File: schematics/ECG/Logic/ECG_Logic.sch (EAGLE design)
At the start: 77 parts, among them IC1 ADS1293, IC10 FSA4157, IC2 LIS3DH, IC3 MCP1703, IC4 CC2541, IC5 FSA4157, IC6 FSA4157, IC7 FSA4157, IC8 BALUN_2450BM_SERIES_SMD, IC9 LTC6907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

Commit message: added board detect pin, need to find proper place to route trace
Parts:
- added U$7: TARGET_RA, pins:TARGET_RA
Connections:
- new net BOARD_DETECT: U$7.1
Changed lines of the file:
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@@
 <grid distance="0.1" unitdist="inch" unit="inch" style="lines" multiple="1" display="no" altdistance="0.01" altunitdist="inch" altunit="inch"/>
 <layers>
-<layer number="1" name="Top" color="4" fill="1" visible="yes" active="no"/>
-<layer number="2" name="Route2" color="1" fill="3" visible="yes" active="no"/>
-<layer number="3" name="Route3" color="4" fill="3" visible="yes" active="no"/>
-<layer number="4" name="Route4" color="1" fill="4" visible="yes" active="no"/>
-<layer number="5" name="Route5" color="4" fill="4" visible="yes" active="no"/>
-<layer number="6" name="Route6" color="1" fill="8" visible="yes" active="no"/>
-<layer number="7" name="Route7" color="4" fill="8" visible="yes" active="no"/>
-<layer number="8" name="Route8" color="1" fill="2" visible="yes" active="no"/>
-<layer number="9" name="Route9" color="4" fill="2" visible="yes" active="no"/>
-<layer number="10" name="Route10" color="1" fill="7" visible="yes" active="no"/>
-<layer number="11" name="Route11" color="4" fill="7" visible="yes" active="no"/>
-<layer number="12" name="Route12" color="1" fill="5" visible="yes" active="no"/>
-<layer number="13" name="Route13" color="4" fill="5" visible="yes" active="no"/>
-<layer number="14" name="Route14" color="1" fill="6" visible="yes" active="no"/>
-<layer number="15" name="Route15" color="4" fill="6" visible="yes" active="no"/>
-<layer number="16" name="Bottom" color="1" fill="1" visible="yes" active="no"/>
-<layer number="17" name="Pads" color="2" fill="1" visible="yes" active="no"/>
-<layer number="18" name="Vias" color="2" fill="1" visible="yes" active="no"/>
-<layer number="19" name="Unrouted" color="6" fill="1" visible="yes" active="no"/>
-<layer number="20" name="Dimension" color="15" fill="1" visible="yes" active="no"/>
-<layer number="21" name="tPlace" color="7" fill="1" visible="yes" active="no"/>
-<layer number="22" name="bPlace" color="7" fill="1" visible="yes" active="no"/>
-<layer number="23" name="tOrigins" color="15" fill="1" visible="yes" active="no"/>
-<layer number="24" name="bOrigins" color="15" fill="1" visible="yes" active="no"/>
-<layer number="25" name="tNames" color="7" fill="1" visible="yes" active="no"/>
-<layer number="26" name="bNames" color="7" fill="1" visible="yes" active="no"/>
-<layer number="27" name="tValues" color="7" fill="1" visible="yes" active="no"/>
-<layer number="28" name="bValues" color="7" fill="1" visible="yes" active="no"/>
+<layer number="1" name="Top" color="4" fill="1" visible="no" active="no"/>
+<layer number="2" name="Route2" color="1" fill="3" visible="no" active="no"/>
+<layer number="3" name="Route3" color="4" fill="3" visible="no" active="no"/>
+<layer number="4" name="Route4" color="1" fill="4" visible="no" active="no"/>
+<layer number="5" name="Route5" color="4" fill="4" visible="no" active="no"/>
+<layer number="6" name="Route6" color="1" fill="8" visible="no" active="no"/>
+<layer number="7" name="Route7" color="4" fill="8" visible="no" active="no"/>
+<layer number="8" name="Route8" color="1" fill="2" visible="no" active="no"/>
+<layer number="9" name="Route9" color="4" fill="2" visible="no" active="no"/>
+<layer number="10" name="Route10" color="1" fill="7" visible="no" active="no"/>
+<layer number="11" name="Route11" color="4" fill="7" visible="no" active="no"/>
+<layer number="12" name="Route12" color="1" fill="5" visible="no" active="no"/>
+<layer number="13" name="Route13" color="4" fill="5" visible="no" active="no"/>
+<layer number="14" name="Route14" color="1" fill="6" visible="no" active="no"/>
+<layer number="15" name="Route15" color="4" fill="6" visible="no" active="no"/>
+<layer number="16" name="Bottom" color="1" fill="1" visible="no" active="no"/>
+<layer number="17" name="Pads" color="2" fill="1" visible="no" active="no"/>
+<layer number="18" name="Vias" color="2" fill="1" visible="no" active="no"/>
+<layer number="19" name="Unrouted" color="6" fill="1" visible="no" active="no"/>
+<layer number="20" name="Dimension" color="15" fill="1" visible="no" active="no"/>
+<layer number="21" name="tPlace" color="7" fill="1" visible="no" active="no"/>
+<layer number="22" name="bPlace" color="7" fill="1" visible="no" active="no"/>
+<layer number="23" name="tOrigins" color="15" fill="1" visible="no" active="no"/>
+<layer number="24" name="bOrigins" color="15" fill="1" visible="no" active="no"/>
+<layer number="25" name="tNames" color="7" fill="1" visible="no" active="no"/>
+<layer number="26" name="bNames" color="7" fill="1" visible="no" active="no"/>
+<layer number="27" name="tValues" color="7" fill="1" visible="no" active="no"/>
+<layer number="28" name="bValues" color="7" fill="1" visible="no" active="no"/>
 <layer number="29" name="tStop" color="7" fill="3" visible="no" active="no"/>
 <layer number="30" name="bStop" color="7" fill="6" visible="no" active="no"/>
@@
 <layer number="35" name="tGlue" color="7" fill="4" visible="no" active="no"/>
 <layer number="36" name="bGlue" color="7" fill="5" visible="no" active="no"/>
-<layer number="37" name="tTest" color="7" fill="1" visible="yes" active="no"/>
-<layer number="38" name="bTest" color="7" fill="1" visible="yes" active="no"/>
+<layer number="37" name="tTest" color="7" fill="1" visible="no" active="no"/>
+<layer number="38" name="bTest" color="7" fill="1" visible="no" active="no"/>
 <layer number="39" name="tKeepout" color="4" fill="11" visible="no" active="no"/>
 <layer number="40" name="bKeepout" color="1" fill="11" visible="no" active="no"/>
@@
 <layer number="44" name="Drills" color="7" fill="1" visible="no" active="no"/>
 <layer number="45" name="Holes" color="7" fill="1" visible="no" active="no"/>
-<layer number="46" name="Milling" color="3" fill="1" visible="yes" active="no"/>
-<layer number="47" name="Measures" color="7" fill="1" visible="yes" active="no"/>
-<layer number="48" name="Document" color="7" fill="1" visible="yes" active="no"/>
-<layer number="49" name="Reference" color="7" fill="1" visible="yes" active="no"/>
-<layer number="50" name="dxf" color="7" fill="1" visible="yes" active="no"/>
-<layer number="51" name="tDocu" color="7" fill="1" visible="yes" active="no"/>
-<layer number="52" name="bDocu" color="7" fill="1" visible="yes" active="no"/>
-<layer number="53" name="tGND_GNDA" color="7" fill="9" visible="yes" active="no"/>
-<layer number="54" name="bGND_GNDA" color="1" fill="9" visible="yes" active="no"/>
-<layer number="56" name="wert" color="7" fill="1" visible="yes" active="no"/>
+<layer number="46" name="Milling" color="3" fill="1" visible="no" active="no"/>
+<layer number="47" name="Measures" color="7" fill="1" visible="no" active="no"/>
+<layer number="48" name="Document" color="7" fill="1" visible="no" active="no"/>
+<layer number="49" name="Reference" color="7" fill="1" visible="no" active="no"/>
+<layer number="50" name="dxf" color="7" fill="1" visible="no" active="no"/>
+<layer number="51" name="tDocu" color="7" fill="1" visible="no" active="no"/>
+<layer number="52" name="bDocu" color="7" fill="1" visible="no" active="no"/>
+<layer number="53" name="tGND_GNDA" color="7" fill="9" visible="no" active="no"/>
+<layer number="54" name="bGND_GNDA" color="1" fill="9" visible="no" active="no"/>
+<layer number="56" name="wert" color="7" fill="1" visible="no" active="no"/>
 <layer number="91" name="Nets" color="2" fill="1" visible="yes" active="yes"/>
 <layer number="92" name="Busses" color="1" fill="1" visible="yes" active="yes"/>
@@
 <part name="IC10" library="fairchild" deviceset="FSA4157" device=""/>
 <part name="GND17" library="supply1" deviceset="GND" device=""/>
+<part name="U$7" library="pins" deviceset="TARGET_RA" device=""/>
 </parts>
 <sheets>
@@
 <instance part="IC10" gate="FSA4157" x="68.58" y="162.56"/>
 <instance part="GND17" gate="1" x="55.88" y="157.48"/>
+<instance part="U$7" gate="PIN" x="187.96" y="187.96"/>
 </instances>
 <busses>
@@
 </segment>
 </net>
+<net name="BOARD_DETECT" class="0">
+<segment>
+<pinref part="U$7" gate="PIN" pin="1"/>
+<wire x1="182.88" y1="187.96" x2="180.34" y2="187.96" width="0.1524" layer="91"/>
+<junction x="182.88" y="187.96"/>
+<label x="165.1" y="187.96" size="1.27" layer="95"/>
+</segment>
+</net>

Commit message: routed detect pin to cc2541
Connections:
- net BOARD_DETECT: now also IC4.SCL
- net OSC_SW_VCC: now also IC4.SDA; no longer IC4.SCL
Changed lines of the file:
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@@
 <?xml version="1.0" encoding="utf-8"?>
 <!DOCTYPE eagle SYSTEM "eagle.dtd">
-<eagle version="6.4">
+<eagle version="6.5.0">
 <drawing>
 <settings>
@@
 <net name="OSC_SW_VCC" class="0">
 <segment>
+<pinref part="IC10" gate="FSA4157" pin="S"/>
+<junction x="81.28" y="165.1"/>
+<wire x1="81.28" y1="165.1" x2="83.82" y2="165.1" width="0.1524" layer="91"/>
+<label x="83.82" y="165.1" size="1.27" layer="95"/>
+</segment>
+<segment>
+<pinref part="IC4" gate="G$1" pin="SDA"/>
+<wire x1="205.74" y1="76.2" x2="203.2" y2="76.2" width="0.1524" layer="91"/>
+<junction x="205.74" y="76.2"/>
+<label x="190.5" y="76.2" size="1.27" layer="95"/>
+</segment>
+</net>
+<net name="OSC_VCC" class="0">
+<segment>
+<pinref part="C1" gate="G$1" pin="1"/>
+<wire x1="147.32" y1="137.16" x2="144.78" y2="137.16" width="0.1524" layer="91"/>
+<junction x="147.32" y="137.16"/>
+<label x="137.16" y="137.16" size="1.27" layer="95"/>
+</segment>
+<segment>
+<pinref part="IC9" gate="IC" pin="V+"/>
+<wire x1="134.62" y1="116.84" x2="132.08" y2="116.84" width="0.1524" layer="91"/>
+<junction x="134.62" y="116.84"/>
+<label x="124.46" y="116.84" size="1.27" layer="95"/>
+</segment>
+<segment>
+<pinref part="IC10" gate="FSA4157" pin="A"/>
+<junction x="81.28" y="160.02"/>
+<wire x1="81.28" y1="160.02" x2="83.82" y2="160.02" width="0.1524" layer="91"/>
+<label x="83.82" y="160.02" size="1.27" layer="95"/>
+</segment>
+</net>
+<net name="BOARD_DETECT" class="0">
+<segment>
+<pinref part="U$7" gate="PIN" pin="1"/>
+<wire x1="182.88" y1="187.96" x2="180.34" y2="187.96" width="0.1524" layer="91"/>
+<junction x="182.88" y="187.96"/>
+<label x="165.1" y="187.96" size="1.27" layer="95"/>
+</segment>
+<segment>
 <pinref part="IC4" gate="G$1" pin="SCL"/>
 <wire x1="205.74" y1="78.74" x2="203.2" y2="78.74" width="0.1524" layer="91"/>
@@
 <label x="190.5" y="78.74" size="1.27" layer="95"/>
 </segment>
-<segment>
-<pinref part="IC10" gate="FSA4157" pin="S"/>
-<junction x="81.28" y="165.1"/>
-<wire x1="81.28" y1="165.1" x2="83.82" y2="165.1" width="0.1524" layer="91"/>
-<label x="83.82" y="165.1" size="1.27" layer="95"/>
-</segment>
-</net>
-<net name="OSC_VCC" class="0">
-<segment>
-<pinref part="C1" gate="G$1" pin="1"/>
-<wire x1="147.32" y1="137.16" x2="144.78" y2="137.16" width="0.1524" layer="91"/>
-<junction x="147.32" y="137.16"/>
-<label x="137.16" y="137.16" size="1.27" layer="95"/>
-</segment>
-<segment>
-<pinref part="IC9" gate="IC" pin="V+"/>
-<wire x1="134.62" y1="116.84" x2="132.08" y2="116.84" width="0.1524" layer="91"/>
-<junction x="134.62" y="116.84"/>
-<label x="124.46" y="116.84" size="1.27" layer="95"/>
-</segment>
-<segment>
-<pinref part="IC10" gate="FSA4157" pin="A"/>
-<junction x="81.28" y="160.02"/>
-<wire x1="81.28" y1="160.02" x2="83.82" y2="160.02" width="0.1524" layer="91"/>
-<label x="83.82" y="160.02" size="1.27" layer="95"/>
-</segment>
-</net>
-<net name="BOARD_DETECT" class="0">
-<segment>
-<pinref part="U$7" gate="PIN" pin="1"/>
-<wire x1="182.88" y1="187.96" x2="180.34" y2="187.96" width="0.1524" layer="91"/>
-<junction x="182.88" y="187.96"/>
-<label x="165.1" y="187.96" size="1.27" layer="95"/>
-</segment>
-</net>
+</net>

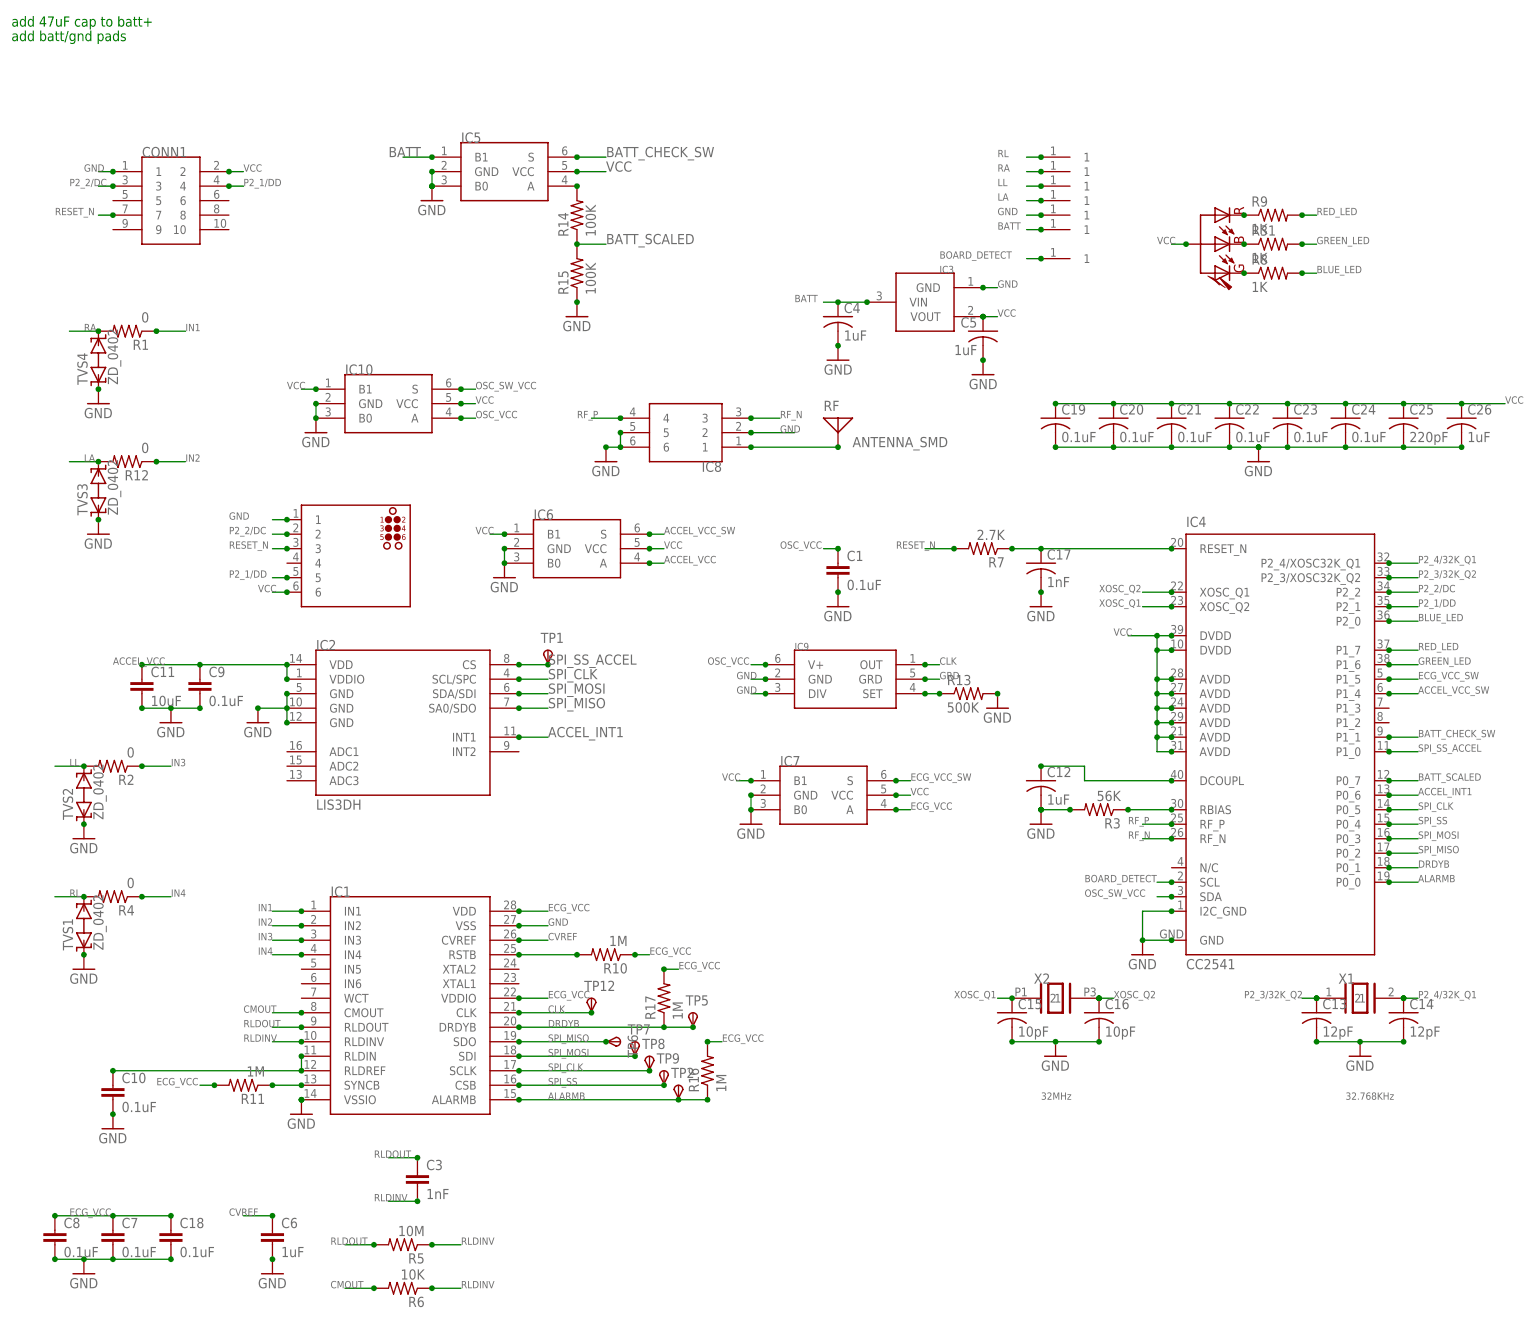
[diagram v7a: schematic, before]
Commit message: added new low profile 4Mhz xtal
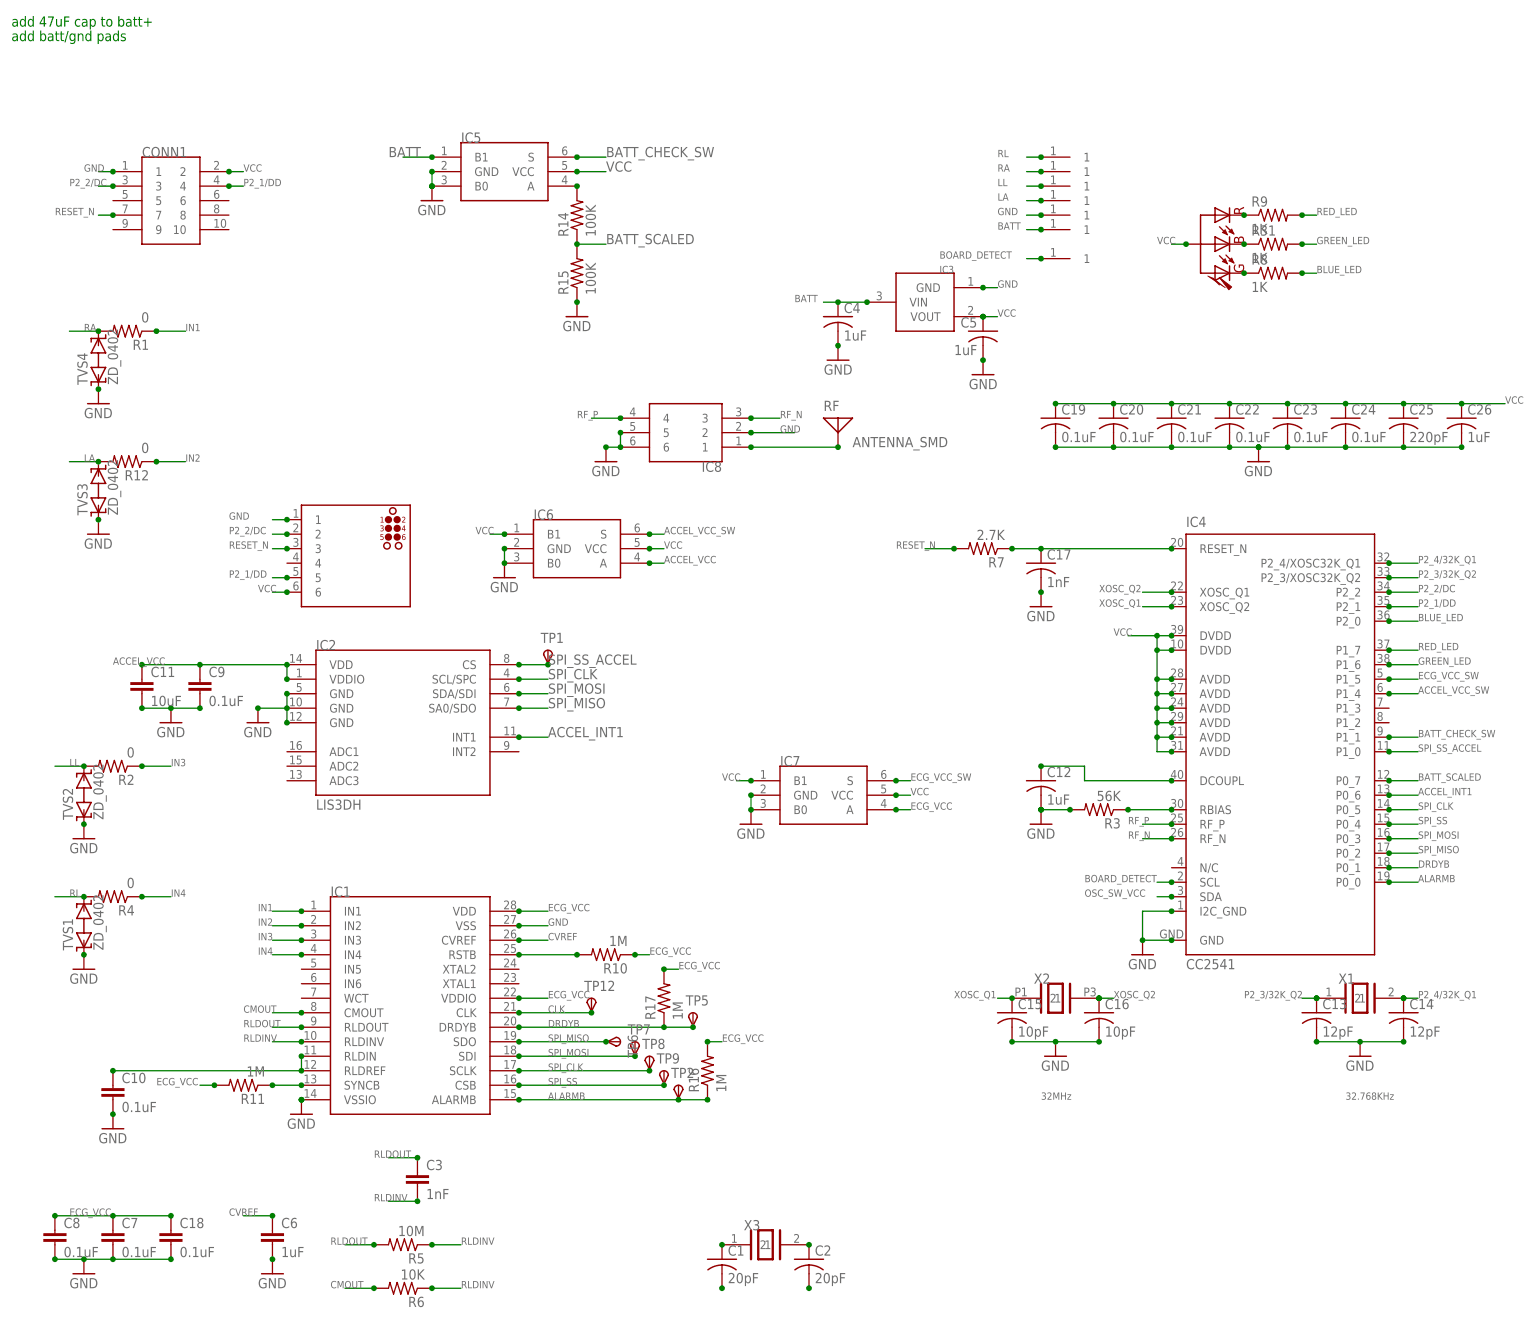
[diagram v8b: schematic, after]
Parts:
- removed IC10: FSA4157, fairchild:FSA4157
- removed IC9: LTC6907, linear:LTC6907
- removed R13: 500K, rcl:R-US_R1206
- added C2: 20pF, rcl:C-USC0201
- added X3: ECS-40-20-4VX, ecs:ECS-40-20-4VX
- C1: value 0.1uF -> 20pF; device rcl:C-EUC0201 -> rcl:C-USC0201
- TP12: value TPSTP11R -> TPSTP06R; device testpad:TPSTP11R -> testpad:TPSTP06R
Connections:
- removed net GRD: IC9.GRD
- removed net N$14: IC9.SET, R13.1
- removed net OSC_VCC: C1.1, IC10.A, IC9.V+
- new net N$1: C1.1, X3.1
- new net N$10: C1.2
- new net N$2: C2.1, X3.2
- new net N$7: C2.2
- net CLK: no longer IC9.OUT
- net GND: no longer C1.2, IC10.B0, IC10.GND, IC9.DIV, IC9.GND, R13.2
- net OSC_SW_VCC: no longer IC10.S
- net VCC: no longer IC10.B1, IC10.VCC
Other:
- moved on the sheet: C1
